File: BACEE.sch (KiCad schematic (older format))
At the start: 13 parts, among them U1 24LC1025, U2 DS1337S+, U3 24LC1025, U4 ATMEGA328P-AU, Y1 Crystal 32768 kHz, Y2 Crystal 16MHz

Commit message: Adjusted designators, units etc as per Larry's feedback.
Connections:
- net labels added: GNDPWR
- net labels removed: GND
- wire segments 87 -> 88
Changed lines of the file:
@@
-	1    0    0    -1
-$EndComp
-$Comp
-L power:GND #PWR02
-U 1 1 5B7FDCEB
-P 10000 3250
-F 0 "#PWR02" H 10000 3000 50  0001 C CNN
-F 1 "GND" H 10005 3077 50  0000 C CNN
-F 2 "" H 10000 3250 50  0001 C CNN
-F 3 "" H 10000 3250 50  0001 C CNN
-	1    10000 3250
 	1    0    0    -1
 $EndComp
@@
 F17 "TX" O L 3550 5400 50
 $EndSheet
-$Comp
-L power:GND #PWR01
-U 1 1 5B7FEA2F
-P 2950 5150
-F 0 "#PWR01" H 2950 4900 50  0001 C CNN
-F 1 "GND" H 2955 4977 50  0000 C CNN
-F 2 "" H 2950 5150 50  0001 C CNN
-F 3 "" H 2950 5150 50  0001 C CNN
-	1    2950 5150
-	1    0    0    -1
-$EndComp
 Text Label 3450 5050 2    50   ~ 0
 Vcc
@@
 Wire Wire Line
 	6750 2500 6750 2350
-$Comp
-L power:GND #PWR0101
-U 1 1 5B805229
-P 5750 2650
-F 0 "#PWR0101" H 5750 2400 50  0001 C CNN
-F 1 "GND" H 5755 2477 50  0000 C CNN
-F 2 "" H 5750 2650 50  0001 C CNN
-F 3 "" H 5750 2650 50  0001 C CNN
-	1    5750 2650
-	1    0    0    -1
-$EndComp
 Wire Wire Line
 	6750 1950 6300 1950
@@
 Wire Wire Line
 	6100 3200 6100 3450
-$Comp
-L power:GND #PWR0102
-U 1 1 5B806E4B
-P 6100 3950
-F 0 "#PWR0102" H 6100 3700 50  0001 C CNN
-F 1 "GND" H 6105 3777 50  0000 C CNN
-F 2 "" H 6100 3950 50  0001 C CNN
-F 3 "" H 6100 3950 50  0001 C CNN
-	1    6100 3950
-	1    0    0    -1
-$EndComp
 Wire Wire Line
 	6100 3750 6100 3950
@@
 NoConn ~ 7650 4300
 NoConn ~ 7650 4500
-$Comp
-L power:GND #PWR0103
-U 1 1 5B811509
-P 8250 4950
-F 0 "#PWR0103" H 8250 4700 50  0001 C CNN
-F 1 "GND" H 8255 4777 50  0000 C CNN
-F 2 "" H 8250 4950 50  0001 C CNN
-F 3 "" H 8250 4950 50  0001 C CNN
-	1    8250 4950
-	1    0    0    -1
-$EndComp
 Wire Wire Line
 	8150 4800 8150 4900
@@
 Text Label 4300 3700 2    50   ~ 0
 ADDS2
-$Comp
-L power:GND #PWR0104
-U 1 1 5B8142A1
-P 4100 2450
-F 0 "#PWR0104" H 4100 2200 50  0001 C CNN
-F 1 "GND" H 4105 2277 50  0000 C CNN
-F 2 "" H 4100 2450 50  0001 C CNN
-F 3 "" H 4100 2450 50  0001 C CNN
-	1    4100 2450
-	1    0    0    -1
-$EndComp
 Wire Wire Line
 	4100 2200 4100 2450
@@
 Wire Wire Line
 	4700 4150 4700 4000
-$Comp
-L power:GND #PWR0105
-U 1 1 5B81A59B
-P 3950 4250
-F 0 "#PWR0105" H 3950 4000 50  0001 C CNN
-F 1 "GND" H 3955 4077 50  0000 C CNN
-F 2 "" H 3950 4250 50  0001 C CNN
-F 3 "" H 3950 4250 50  0001 C CNN
-	1    3950 4250
-	1    0    0    -1
-$EndComp
 Wire Wire Line
 	3950 4250 3950 4150
@@
 Text Label 3450 7050 2    50   ~ 0
 Vcc
-$Comp
-L power:GND #PWR0106
-U 1 1 5B867438
-P 3450 6750
-F 0 "#PWR0106" H 3450 6500 50  0001 C CNN
-F 1 "GND" H 3455 6577 50  0000 C CNN
-F 2 "" H 3450 6750 50  0001 C CNN
-F 3 "" H 3450 6750 50  0001 C CNN
-	1    3450 6750
-	0    1    1    0
-$EndComp
-Wire Wire Line
-	3550 6750 3450 6750
 Wire Wire Line
 	3550 7050 3450 7050
@@
 	1    0    0    -1
 $EndComp
+$Comp
+L power:GNDPWR #PWR?
+U 1 1 5BA0C10F
+P 8250 4950
+F 0 "#PWR?" H 8250 4750 50  0001 C CNN
+F 1 "GNDPWR" H 8254 4796 50  0000 C CNN
+F 2 "" H 8250 4900 50  0001 C CNN
+F 3 "" H 8250 4900 50  0001 C CNN
+	1    8250 4950
+	1    0    0    -1
+$EndComp
+$Comp
+L power:GNDPWR #PWR?
+U 1 1 5BA0C4DE
+P 10000 3250
+F 0 "#PWR?" H 10000 3050 50  0001 C CNN
+F 1 "GNDPWR" H 10004 3096 50  0000 C CNN
+F 2 "" H 10000 3200 50  0001 C CNN
+F 3 "" H 10000 3200 50  0001 C CNN
+	1    10000 3250
+	1    0    0    -1
+$EndComp
+$Comp
+L power:GNDPWR #PWR?
+U 1 1 5BA0C66E
+P 6100 3950
+F 0 "#PWR?" H 6100 3750 50  0001 C CNN
+F 1 "GNDPWR" H 6104 3796 50  0000 C CNN
+F 2 "" H 6100 3900 50  0001 C CNN
+F 3 "" H 6100 3900 50  0001 C CNN
+	1    6100 3950
+	1    0    0    -1
+$EndComp
+$Comp
+L power:GNDPWR #PWR?
+U 1 1 5BA0C9F8
+P 5750 2650
+F 0 "#PWR?" H 5750 2450 50  0001 C CNN
+F 1 "GNDPWR" H 5754 2496 50  0000 C CNN
+F 2 "" H 5750 2600 50  0001 C CNN
+F 3 "" H 5750 2600 50  0001 C CNN
+	1    5750 2650
+	1    0    0    -1
+$EndComp
+$Comp
+L power:GNDPWR #PWR?
+U 1 1 5BA0CB6D
+P 4100 2450
+F 0 "#PWR?" H 4100 2250 50  0001 C CNN
+F 1 "GNDPWR" H 4104 2296 50  0000 C CNN
+F 2 "" H 4100 2400 50  0001 C CNN
+F 3 "" H 4100 2400 50  0001 C CNN
+	1    4100 2450
+	1    0    0    -1
+$EndComp
+$Comp
+L power:GNDPWR #PWR?
+U 1 1 5BA0CCC8
+P 3950 4250
+F 0 "#PWR?" H 3950 4050 50  0001 C CNN
+F 1 "GNDPWR" H 3954 4096 50  0000 C CNN
+F 2 "" H 3950 4200 50  0001 C CNN
+F 3 "" H 3950 4200 50  0001 C CNN
+	1    3950 4250
+	1    0    0    -1
+$EndComp
+$Comp
+L power:GNDPWR #PWR?
+U 1 1 5BA0CF0D
+P 2950 5150
+F 0 "#PWR?" H 2950 4950 50  0001 C CNN
+F 1 "GNDPWR" H 2954 4996 50  0000 C CNN
+F 2 "" H 2950 5100 50  0001 C CNN
+F 3 "" H 2950 5100 50  0001 C CNN
+	1    2950 5150
+	1    0    0    -1
+$EndComp
+$Comp
+L power:GNDPWR #PWR?
+U 1 1 5BA0D30C
+P 3000 6825
+F 0 "#PWR?" H 3000 6625 50  0001 C CNN
+F 1 "GNDPWR" H 3004 6671 50  0000 C CNN
+F 2 "" H 3000 6775 50  0001 C CNN
+F 3 "" H 3000 6775 50  0001 C CNN
+	1    3000 6825
+	1    0    0    -1
+$EndComp
+Wire Wire Line
+	3000 6750 3000 6825
+Wire Wire Line
+	3000 6750 3550 6750
 $EndSCHEMATC

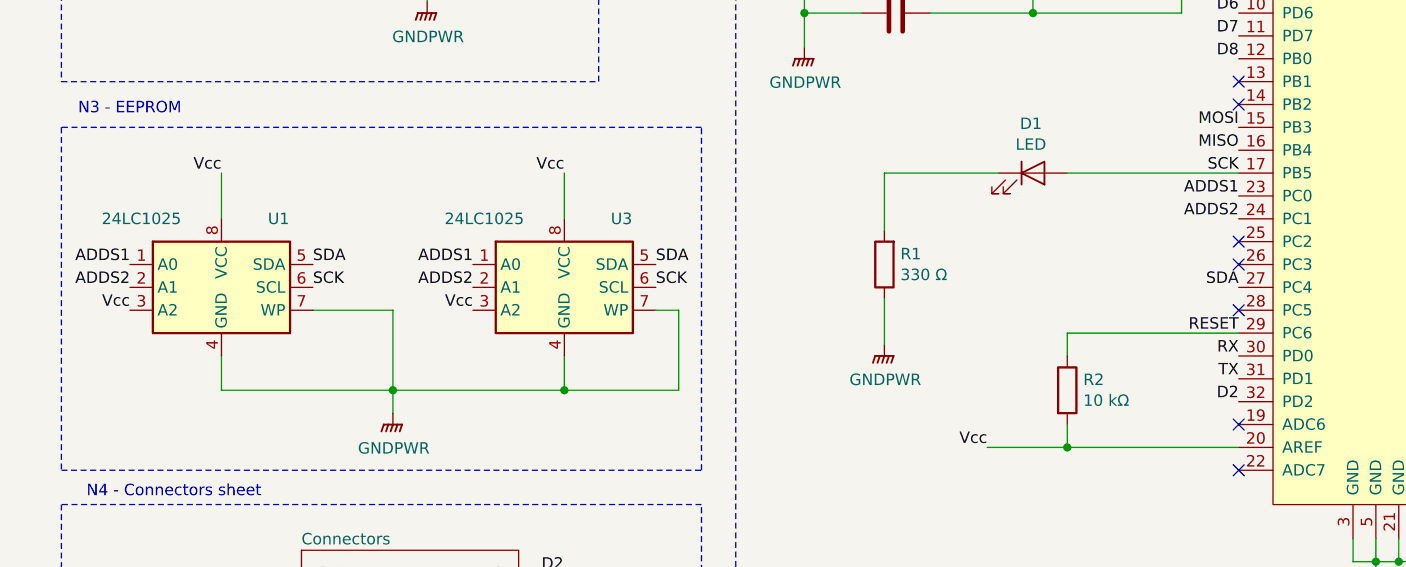
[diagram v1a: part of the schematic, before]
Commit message: Corrected addres pins of EEPROM modules.
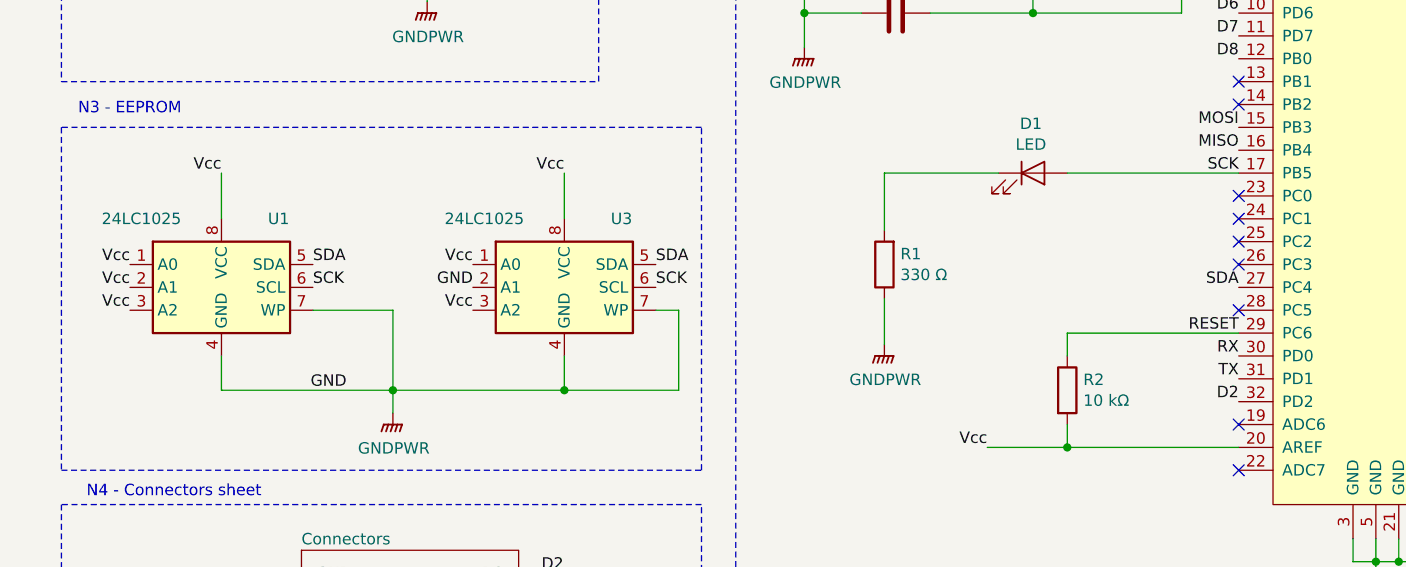
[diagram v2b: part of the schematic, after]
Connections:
- net GNDPWR: now also U3.2 (A1)
- net Vcc: now also U1.1 (A0), U1.2 (A1), U3.1 (A0)
- removed net ADDS1: U1.1 (A0), U3.1 (A0), U4.23 (PC0)
- removed net ADDS2: U1.2 (A1), U3.2 (A1), U4.24 (PC1)
- no-connect marks 8 -> 10
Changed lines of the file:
@@
 Text Label 7650 3200 2    50   ~ 0
 SCK
-Text Label 7650 3300 2    50   ~ 0
-ADDS1
-Text Label 7650 3400 2    50   ~ 0
-ADDS2
 Text Label 7650 3700 2    50   ~ 0
 SDA
@@
 NoConn ~ 7650 2800
 NoConn ~ 7650 2900
-NoConn ~ 7650 3500
 NoConn ~ 7650 3600
 NoConn ~ 7650 3800
@@
 Text Label 5100 3600 0    50   ~ 0
 SDA
-Text Label 2800 3600 2    50   ~ 0
-ADDS1
-Text Label 4300 3600 2    50   ~ 0
-ADDS1
-Text Label 2800 3700 2    50   ~ 0
-ADDS2
-Text Label 4300 3700 2    50   ~ 0
-ADDS2
 Wire Wire Line
 	4100 2200 4100 2450
@@
 	4100 1300 4100 1150
 Text Label 3650 1950 2    50   ~ 0
-Vcc
-Text Label 2800 3800 2    50   ~ 0
-Vcc
-Text Label 4300 3800 2    50   ~ 0
 Vcc
 Text Label 3200 3200 2    50   ~ 0
@@
 Wire Wire Line
 	3000 6750 3550 6750
+NoConn ~ 7650 3500
+NoConn ~ 7650 3400
+NoConn ~ 7650 3300
+Text Label 3590 4150 0    50   ~ 0
+GND
+Text Label 2800 3600 2    50   ~ 0
+Vcc
+Text Label 2800 3700 2    50   ~ 0
+Vcc
+Text Label 2800 3800 2    50   ~ 0
+Vcc
+Text Label 4300 3600 2    50   ~ 0
+Vcc
+Text Label 4300 3800 2    50   ~ 0
+Vcc
+Text Label 4300 3700 2    50   ~ 0
+GND
 $EndSCHEMATC
